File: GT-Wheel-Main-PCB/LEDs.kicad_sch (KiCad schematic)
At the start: 88 parts, among them SW1 56DP30-01-1-AJN, SW10 SKSTAJE010, SW2 56DP30-01-1-AJN, SW3 56DP30-01-1-AJN, SW4 56DP30-01-1-AJN, SW5 SKSTAJE010, SW6 SKSTAJE010, SW7 SKSTAJE010, SW8 SKSTAJE010, SW9 SKSTAJE010

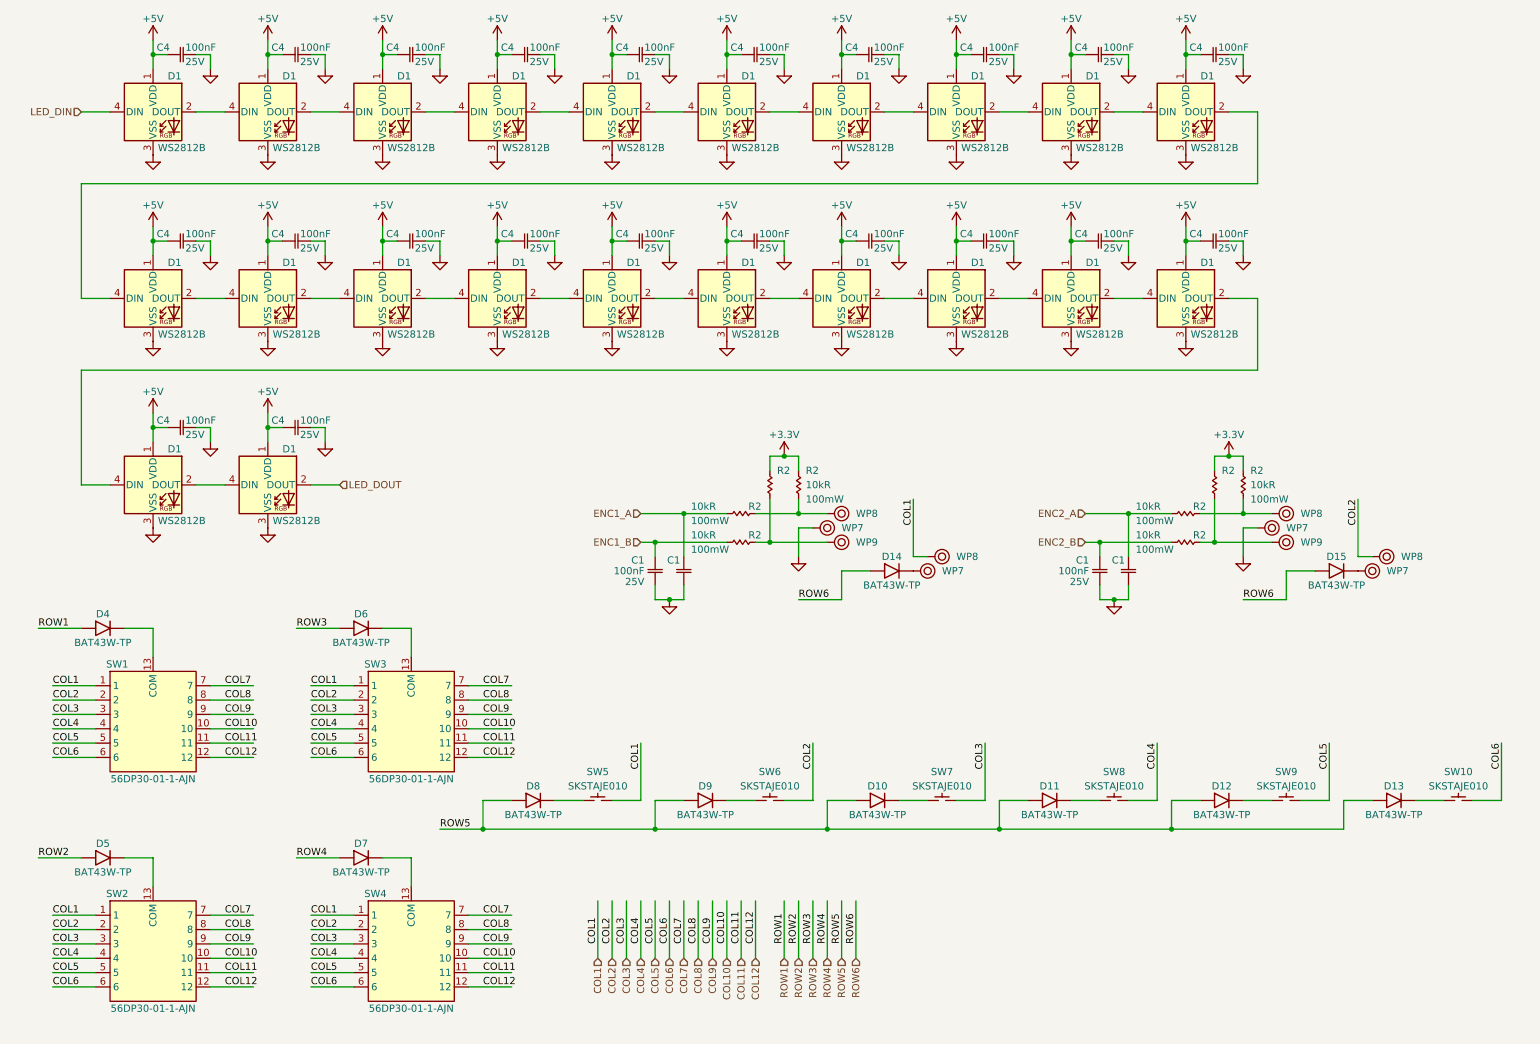
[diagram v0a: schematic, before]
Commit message: removing usb hub
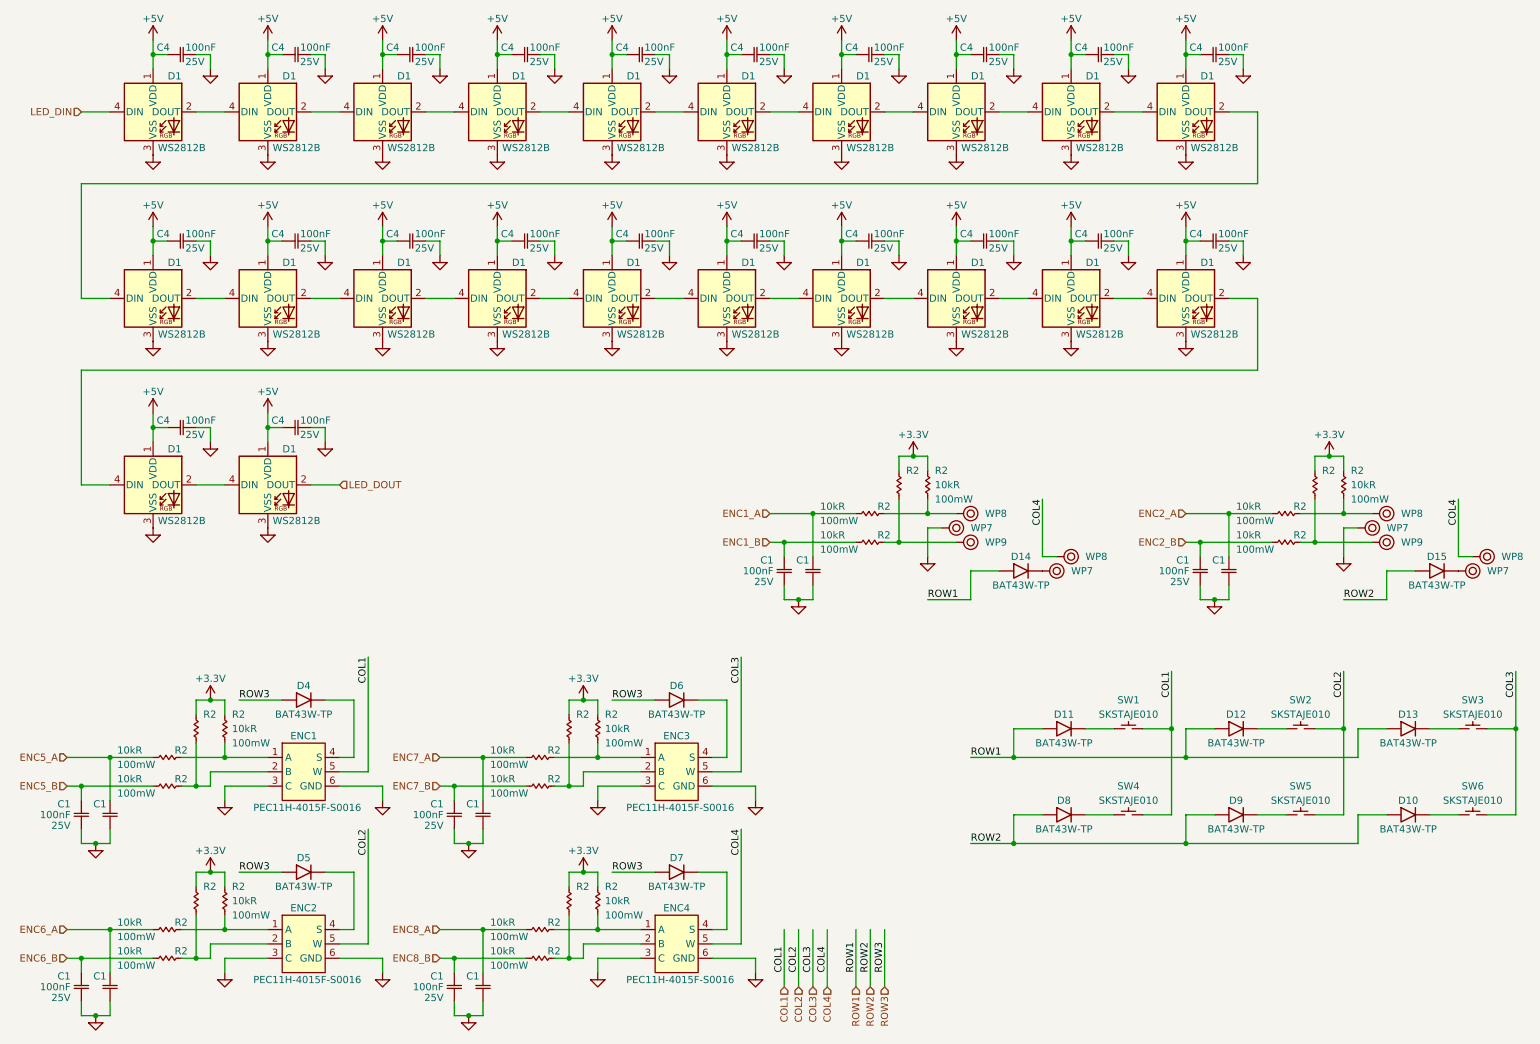
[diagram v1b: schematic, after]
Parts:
- removed SW1, SW2, SW3, SW4: 56DP30-01-1-AJN, SWITCH-THT-ROTARY:56DP30-01-1-AJN, symbol SWITCH-SMD-ROTARY:56DP30-01-1-AJN
- removed SW10, SW7, SW8, SW9: SKSTAJE010, SWITCH-SMD-TACTILE:SKSTAJE010, symbol SWITCH-SMD-TACTILE:SKSTAJE010
- added C1 (x8): 100nF-CER-25V-0402, Capacitor_SMD:C_0402_1005Metric, symbol CAP-SMD-25V:100nF-CER-25V-0402
- added ENC1, ENC2, ENC3, ENC4: PEC11H-4015F-S0016, SWITCH-THT-ENC:PEC11H-4015F-S0016, symbol SWITCH-THT-ENC:PEC11H-4015F-S0016
- added R2 (x16): 10kR-SMD-100mW-0603, Resistor_SMD:R_0603_1608Metric, symbol RES-SMD-100mW:10kR-SMD-100mW-0603
- added SW1, SW2, SW3, SW4: SKSTAJE010, SWITCH-SMD-TACTILE:SKSTAJE010, symbol SWITCH-SMD-TACTILE:SKSTAJE010
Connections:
- net ROW4 is gone; now on net ROW3: D7.2 (A)
- net COL1: now also ENC1.5 (W), SW1.2, SW4.2; no longer SW5.2, WP8.1
- net COL2: now also SW5.2, ENC2.5 (W), SW2.2; no longer SW6.2, WP8.1
- net COL3: now also SW6.2, ENC3.5 (W), SW3.2
- net COL4: now also WP8.1, WP8.1, ENC4.5 (W)
- net LOGIC_GND: now also C1.2, C1.2, C1.2, C1.2, C1.2, C1.2, C1.2, C1.2, ENC1.3 (C), ENC1.6 (GND), ENC2.3 (C), ENC2.6 (GND), ENC3.3 (C), ENC3.6 (GND), ENC4.3 (C), ENC4.6 (GND)
- net ROW1: now also D11.2 (A), D12.2 (A), D13.2 (A), D14.2 (A); no longer D4.2 (A)
- net ROW2: now also D10.2 (A), D15.2 (A), D8.2 (A), D9.2 (A); no longer D5.2 (A)
- net ROW3: now also D4.2 (A), D5.2 (A)
- net at D8.1 (K): now also SW4.1; no longer SW5.1
- net at D9.1 (K): now also SW5.1; no longer SW6.1
- net at D7.1 (K): now also ENC4.4 (S)
- net at D12.1 (K): now also SW2.1
- net at D6.1 (K): now also ENC3.4 (S)
- net at D11.1 (K): now also SW1.1
- net at D5.1 (K): now also ENC2.4 (S)
- net at D10.1 (K): now also SW6.1
- net at D13.1 (K): now also SW3.1
- net at D4.1 (K): now also ENC1.4 (S)
- removed net ROW5: D10.2 (A), D11.2 (A), D12.2 (A), D13.2 (A), D8.2 (A), D9.2 (A)
- removed net ROW6: D14.2 (A), D15.2 (A)
- new net: R2.1, R2.1 (x4)
- new net: ENC3.2 (B), R2.2, R2.2
- new net: ENC2.1 (A), R2.2, R2.2
- new net: ENC1.1 (A), R2.2, R2.2
- new net: ENC2.2 (B), R2.2, R2.2
- new net: ENC1.2 (B), R2.2, R2.2
- new net: ENC3.1 (A), R2.2, R2.2
- new net: ENC4.1 (A), R2.2, R2.2
- new net: ENC4.2 (B), R2.2, R2.2
- new net ENC5_A: C1.1, R2.1
- new net ENC5_B: C1.1, R2.1
- new net ENC6_A: C1.1, R2.1
- new net ENC6_B: C1.1, R2.1
- new net ENC7_A: C1.1, R2.1
- new net ENC7_B: C1.1, R2.1
- new net ENC8_A: C1.1, R2.1
- new net ENC8_B: C1.1, R2.1
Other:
- moved on the sheet: C1, D10, D11, D12, D13, D14, D15, D4, D8, D9, R2, WP7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

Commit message: update
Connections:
- net LOGIC_GND: now also ENC1.2 (C), ENC2.2 (C), ENC3.2 (C), ENC4.2 (C); no longer ENC1.3 (C), ENC2.3 (C), ENC3.3 (C), ENC4.3 (C)
- net +5V: now reaches C4.1, D1.1 (VDD)
- net +5V: now also C4.1, C4.1, C4.1, C4.1, C4.1, C4.1, C4.1, C4.1, C4.1, C4.1, C4.1, C4.1, C4.1, C4.1, C4.1, C4.1, C4.1, C4.1, C4.1, C4.1, C4.1, D1.1 (VDD), D1.1 (VDD), D1.1 (VDD), D1.1 (VDD), D1.1 (VDD), D1.1 (VDD), D1.1 (VDD), D1.1 (VDD), D1.1 (VDD), D1.1 (VDD), D1.1 (VDD), D1.1 (VDD), D1.1 (VDD), D1.1 (VDD), D1.1 (VDD), D1.1 (VDD), D1.1 (VDD), D1.1 (VDD), D1.1 (VDD), D1.1 (VDD), D1.1 (VDD)
- net +3.3V: now reaches R2.1, R2.1
- net +3.3V: now also R2.1, R2.1, R2.1, R2.1, R2.1, R2.1, R2.1, R2.1, R2.1, R2.1
- net at R2.2, R2.2: now also ENC3.3 (B); no longer ENC3.2 (B)
- net at R2.2, R2.2: now also ENC2.3 (B); no longer ENC2.2 (B)
- net at R2.2, R2.2: now also ENC1.3 (B); no longer ENC1.2 (B)
- net at R2.2, R2.2: now also ENC4.3 (B); no longer ENC4.2 (B)
